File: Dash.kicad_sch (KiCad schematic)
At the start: 105 parts, among them J1 Conn_01x03_Socket, J10 Conn_01x03_Socket, J11 Conn_01x04_Socket, J2 Conn_01x03_Socket, J3 Conn_01x03_Socket, J4 Conn_01x03_Socket, J5 Conn_01x03_Socket, J6 Conn_01x03_Socket, J7 Conn_01x07_Socket, J8 Conn_01x06_Socket, J9 Conn_01x05_Socket, Q1 2N7000, Q10 NPN, Q11 NPN, Q12 NPN, Q13 NPN, Q14 NPN, Q15 NPN, Q2 NPN, Q3 NPN, Q4 NPN, Q5 NPN, Q6 NPN, Q7 NPN, Q8 NPN, Q9 NPN, SW1 SW_Push, U1 SFH617A-1, U2 24C02Cx-x-SN, U3 24C02Cx-x-SN, U4 LM2678T-3.3, U5 LM2678T-5.0, U6 ESP32-S2-DevKitM

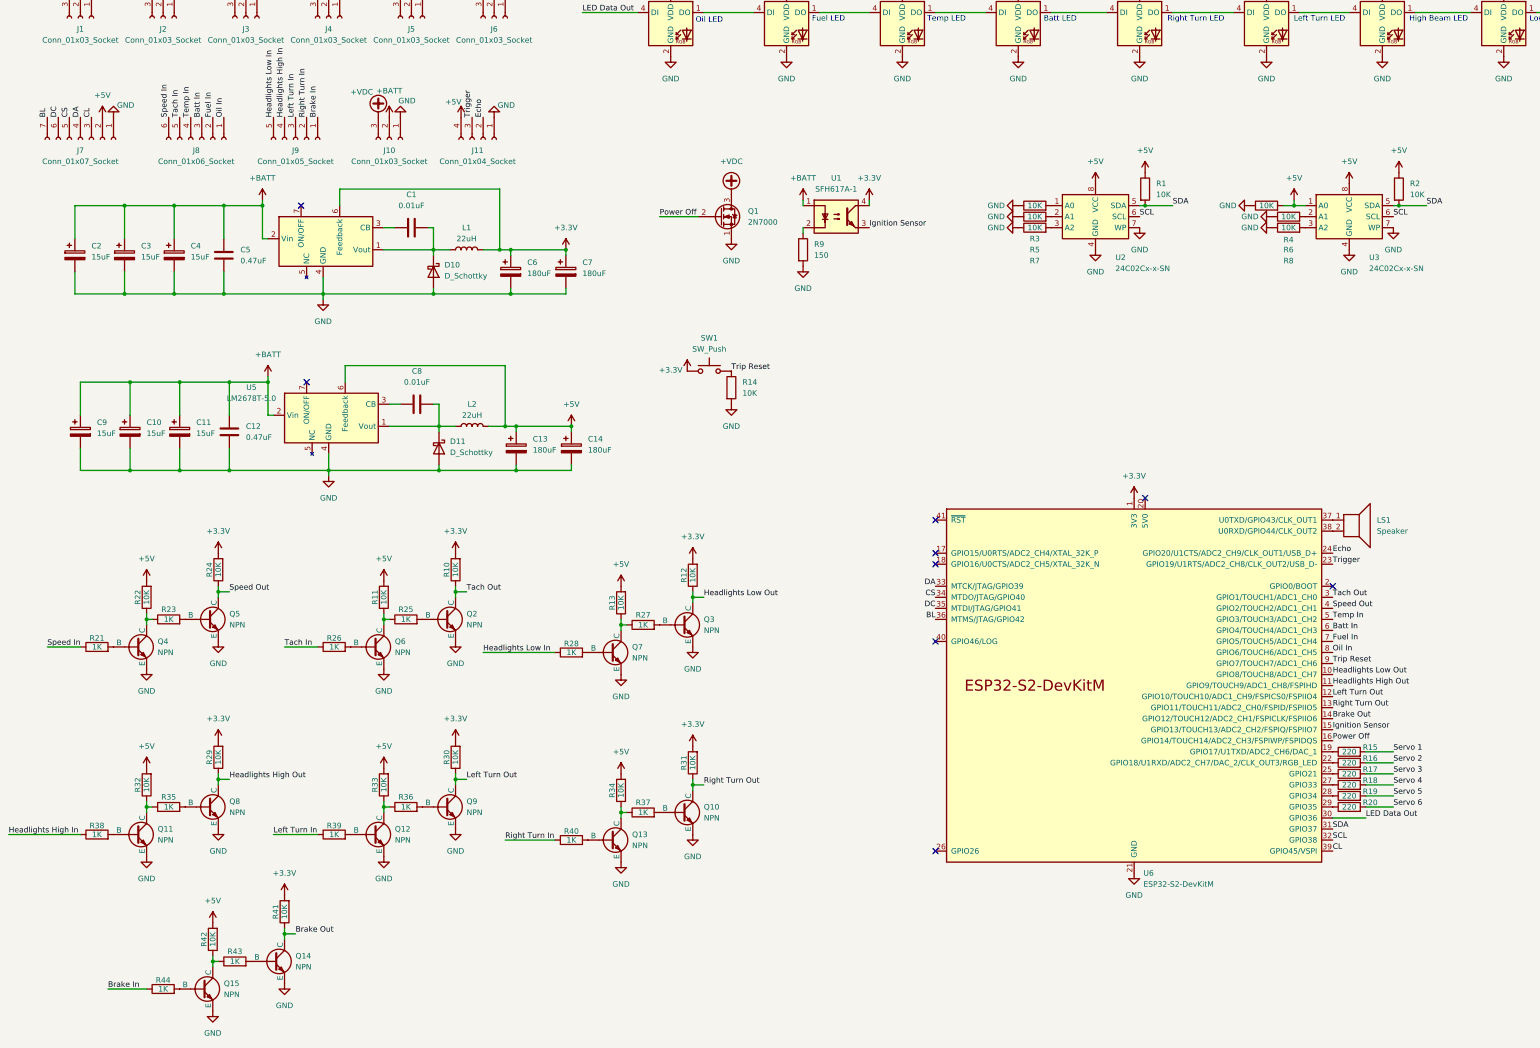
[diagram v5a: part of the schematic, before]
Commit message: Update
Changed logic shifters back to older version, changed names of outputs for clarification, added shifter for echo pin
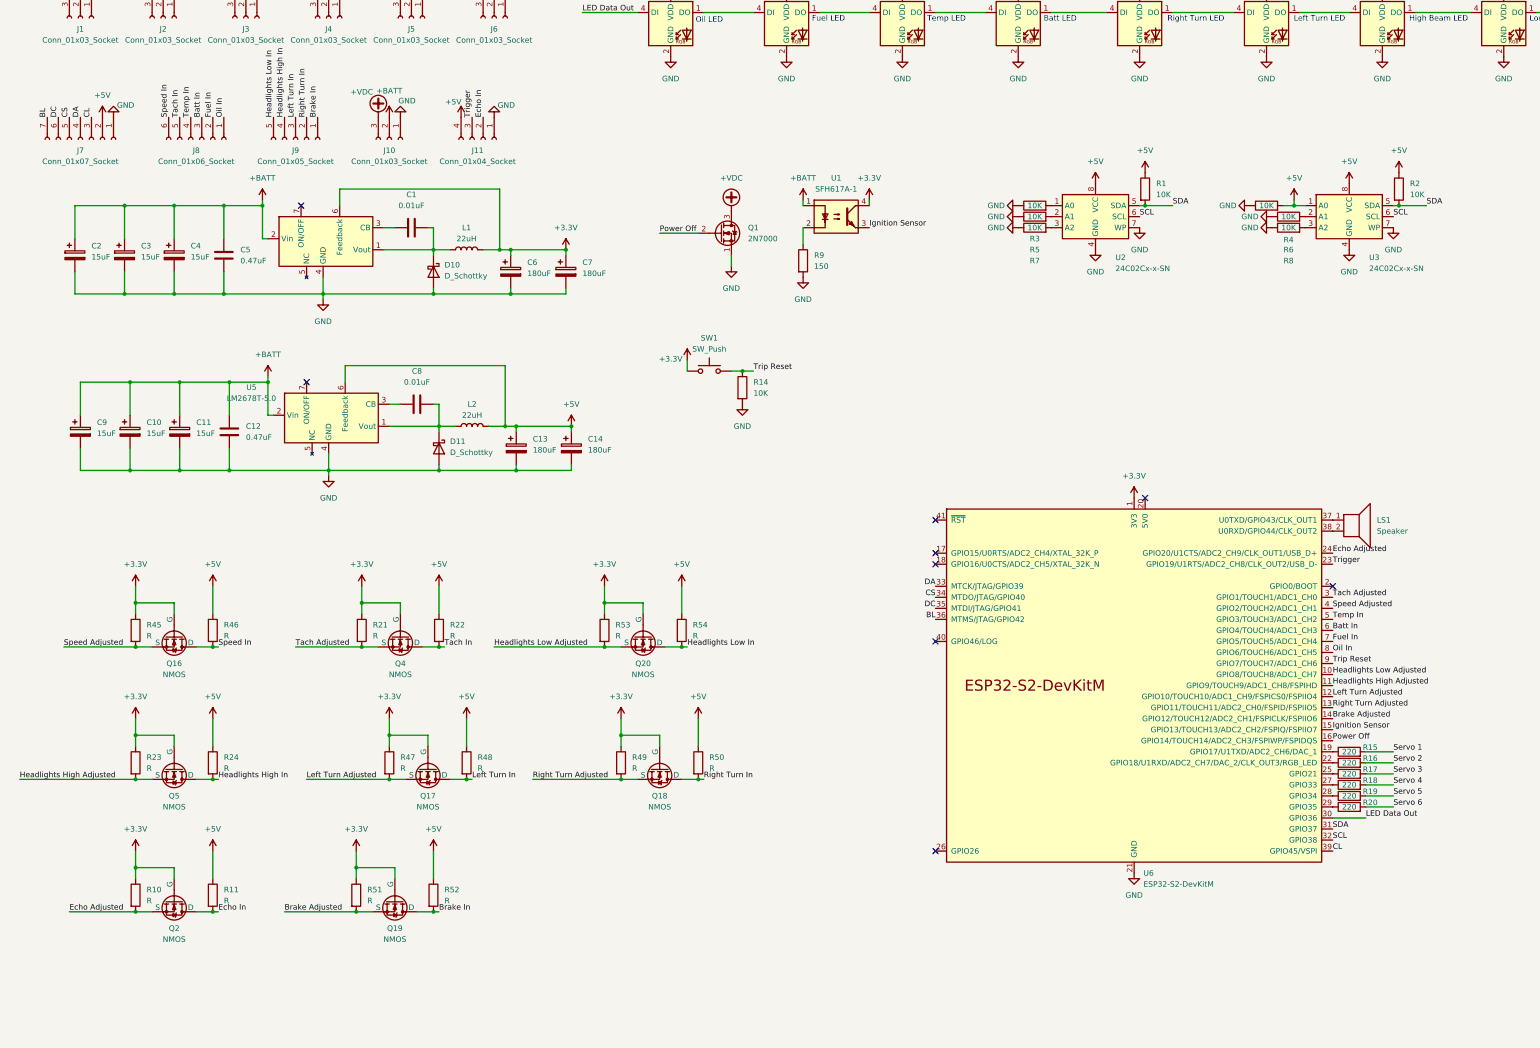
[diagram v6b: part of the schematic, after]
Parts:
- removed Q10, Q11, Q12, Q13, Q14, Q15, Q2, Q3, Q4, Q5, Q6, Q7, Q8, Q9: NPN, symbol Simulation_SPICE:NPN
- removed R12, R13, R29, R30, R31, R32, R33, R34, R41, R42: 10K, symbol Device:R
- removed R25, R26, R27, R28, R35, R36, R37, R38, R39, R40, R43, R44: 1K, symbol Device:R
- added Q16, Q17, Q18, Q19, Q2, Q20, Q4, Q5: NMOS, symbol Simulation_SPICE:NMOS
- added R45, R46, R47, R48, R49, R50, R51, R52, R53, R54: R, symbol Device:R
- R10, R11, R22, R24: value 10K -> R
- R21, R23: value 1K -> R
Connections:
- net Headlights High Out is gone; now on net Headlights High Adjusted: U6.11 (GPIO9/TOUCH9/ADC1_CH8/FSPIHD)
- net +3.3V: now also R10.1, R21.1, R23.1, Q16.2 (G), Q17.2 (G), Q18.2 (G), Q19.2 (G), Q2.2 (G), Q20.2 (G), Q4.2 (G), Q5.2 (G), R45.1, R47.1, R49.1, R51.1, R53.1; no longer R10.2, R24.2
- net +5V: now also R11.1, R22.1, R24.1, R46.1, R48.1, R50.1, R52.1, R54.1; no longer R11.2, R22.2
- net Brake In: now also Q19.1 (D), R52.2
- net Headlights High In: now also R24.2, Q5.1 (D)
- net Headlights Low In: now also Q20.1 (D), R54.2
- net Left Turn In: now also Q17.1 (D), R48.2
- net Right Turn In: now also Q18.1 (D), R50.2
- net Speed In: now also Q16.1 (D), R46.2; no longer R21.1
- net Tach In: now also R22.2, Q4.1 (D)
- net Headlights High Adjusted: now reaches R23.2
- net Headlights High Adjusted: now also Q5.3 (S)
- net Tach Adjusted: now reaches R21.2
- net Tach Adjusted: now also U6.3 (GPIO1/TOUCH1/ADC1_CH0), Q4.3 (S)
- net Brake Out renamed Brake Adjusted
- net Brake Adjusted: now also Q19.3 (S), R51.2
- net Echo renamed Echo Adjusted
- net Echo Adjusted: now also R10.2, Q2.3 (S); no longer J11.2 (Pin_2)
- net Headlights Low Out renamed Headlights Low Adjusted
- net Headlights Low Adjusted: now also Q20.3 (S), R53.2
- net Left Turn Out renamed Left Turn Adjusted
- net Left Turn Adjusted: now also Q17.3 (S), R47.2
- net Right Turn Out renamed Right Turn Adjusted
- net Right Turn Adjusted: now also Q18.3 (S), R49.2
- net Speed Out renamed Speed Adjusted
- net Speed Adjusted: now also Q16.3 (S), R45.2; no longer R24.1
- removed net Tach Out: R10.1, U6.3 (GPIO1/TOUCH1/ADC1_CH0)
- new net Echo In: J11.2 (Pin_2), Q2.1 (D), R11.2
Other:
- moved on the sheet: Q1, R14, R9

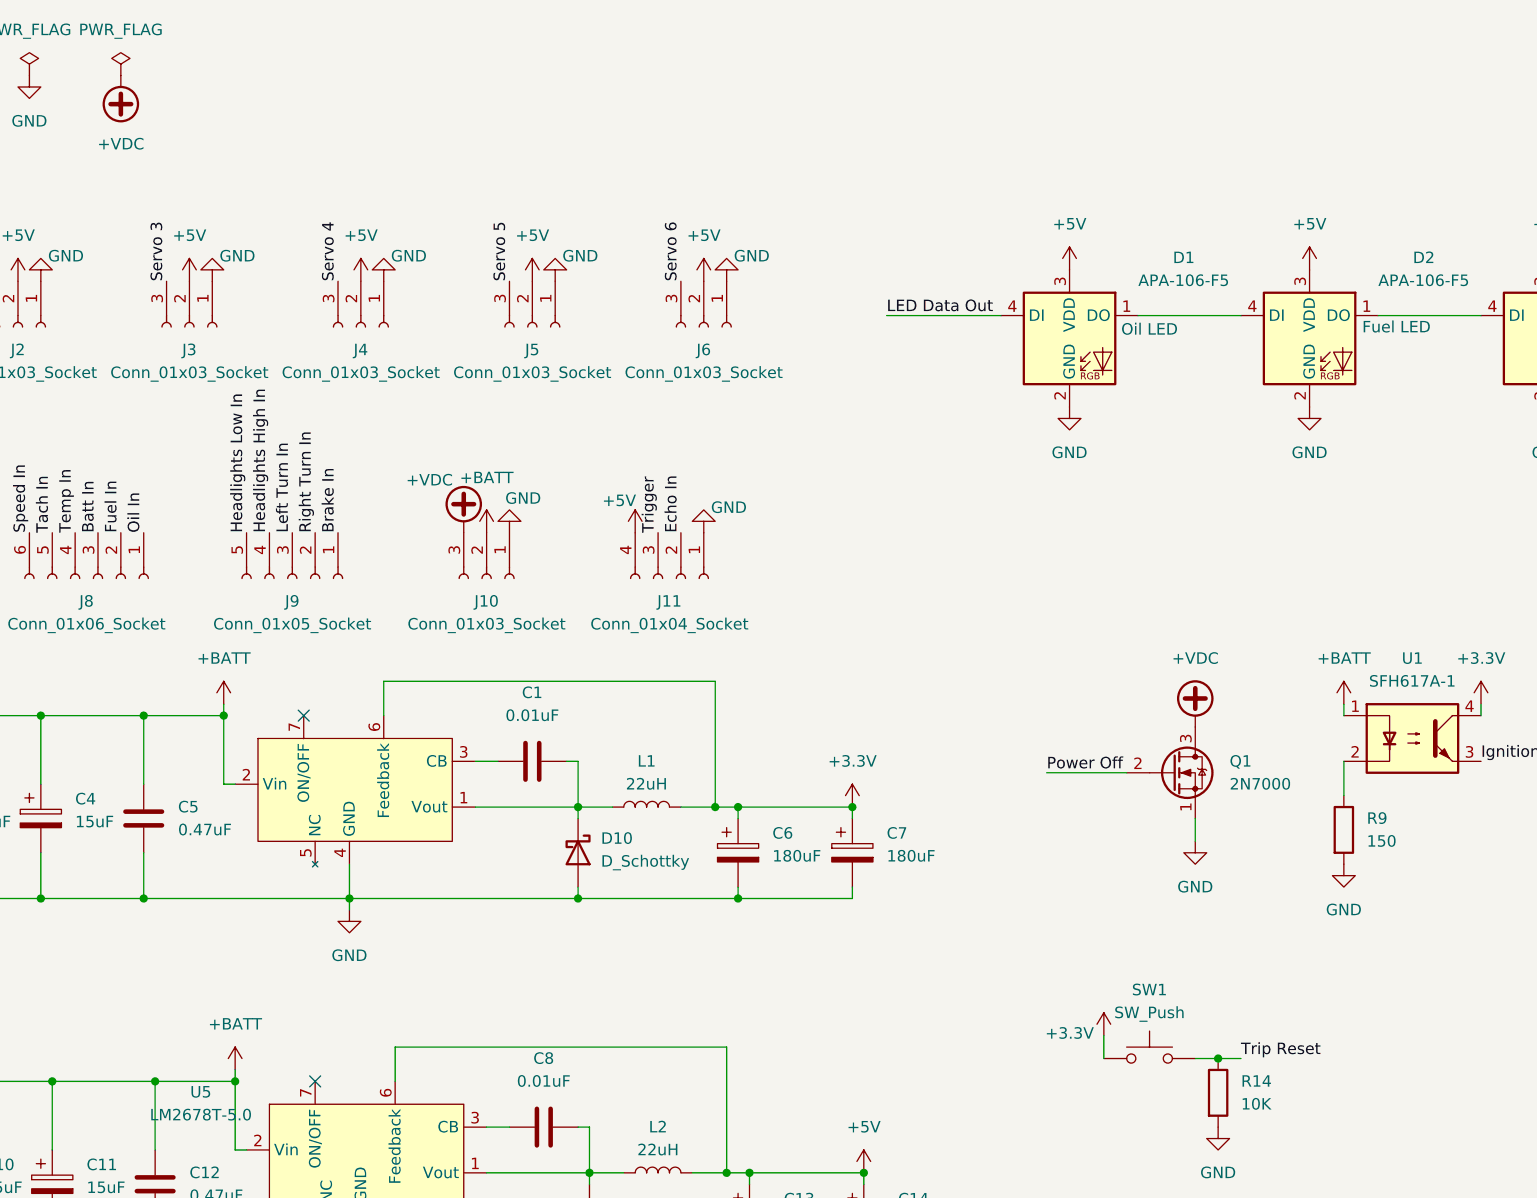
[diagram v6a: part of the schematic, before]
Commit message: Edited power shut off components
Placed diodes on gate of power shut off mosfet, one wired to esp32, other wired to keyed power detection
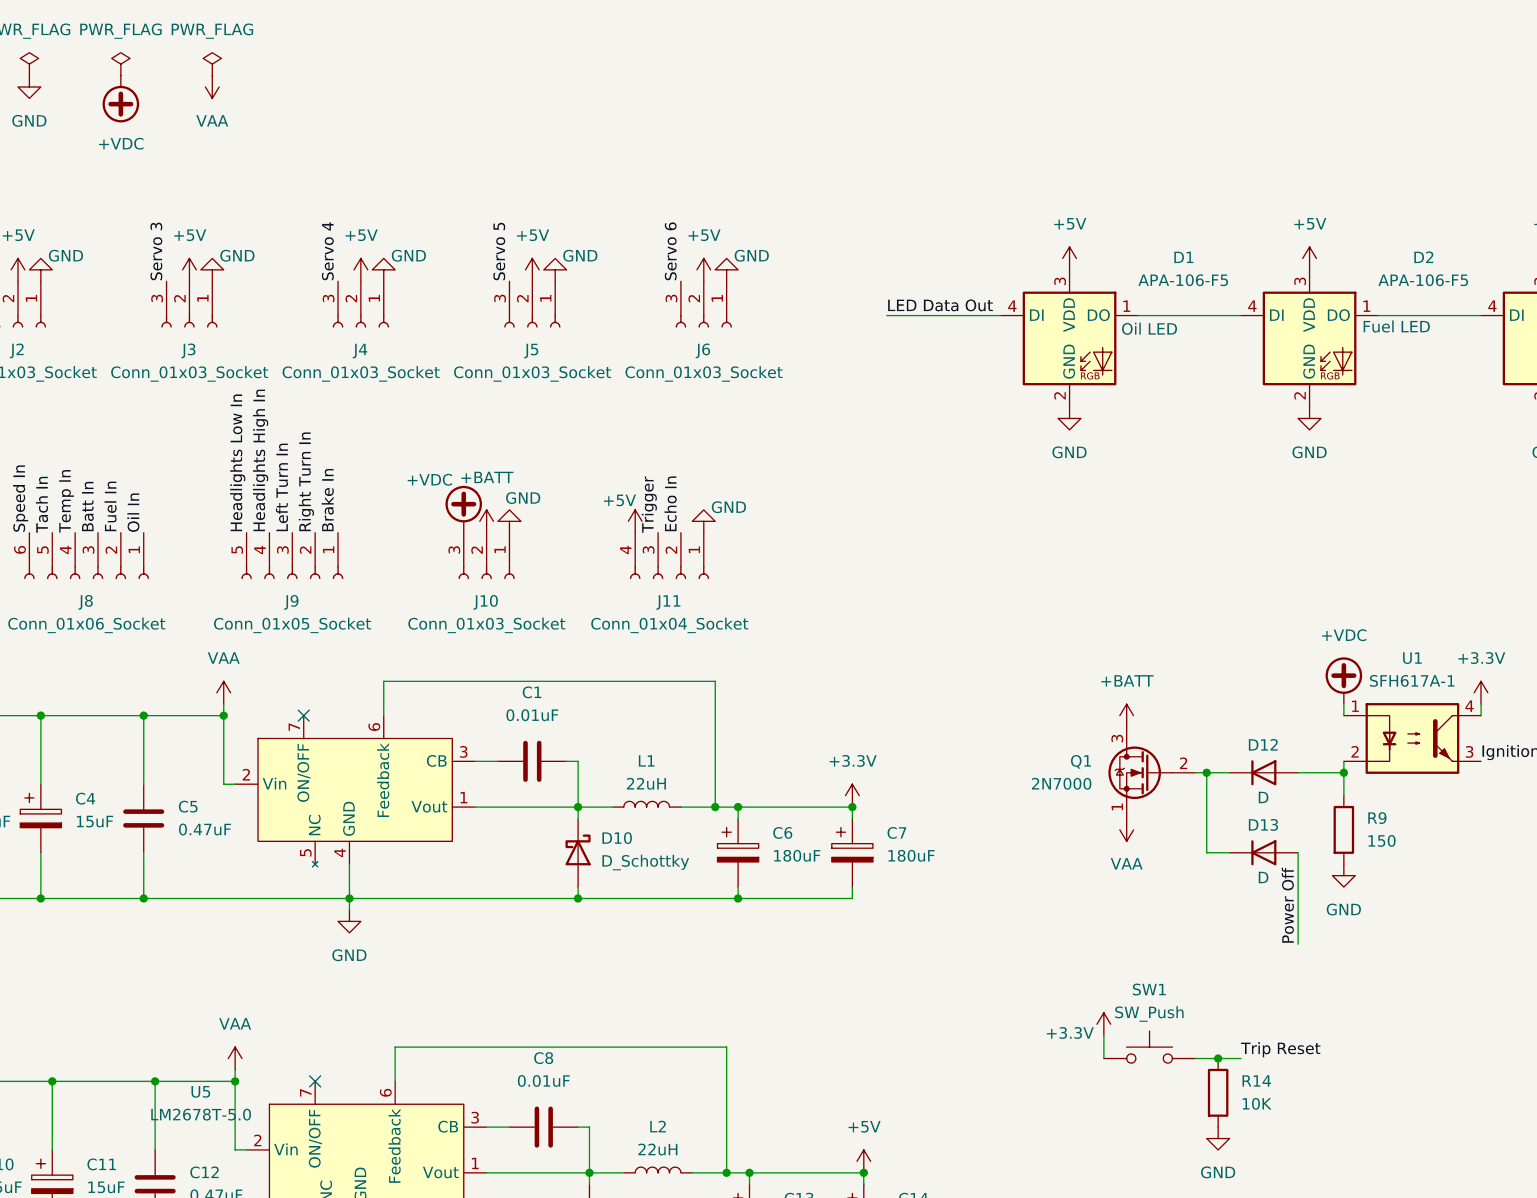
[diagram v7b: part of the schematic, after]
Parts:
- added D12, D13: D, symbol Device:D
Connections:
- net +BATT: now also Q1.3 (D); no longer C10.1, C11.1, C12.1, C2.1, C3.1, C4.1, C5.1, C9.1, U1.1, U4.2 (Vin), U5.2 (Vin)
- net +VDC: now also U1.1; no longer Q1.3 (D)
- net GND: no longer Q1.1 (S)
- net Power Off: now also D13.2 (A); no longer Q1.2 (G)
- net at R9.1, U1.2: now also D12.2 (A)
- new net: D12.1 (K), D13.1 (K), Q1.2 (G)
- new net VAA: C10.1, C11.1, C12.1, C2.1, C3.1, C4.1, C5.1, C9.1, Q1.1 (S), U4.2 (Vin), U5.2 (Vin)
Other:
- moved on the sheet: Q1
